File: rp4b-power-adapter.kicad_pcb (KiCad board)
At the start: 2 copper layers, 78 x 28 mm, 6 parts, among them X1 TYPE-C-31-M-12, X2 FH-00339

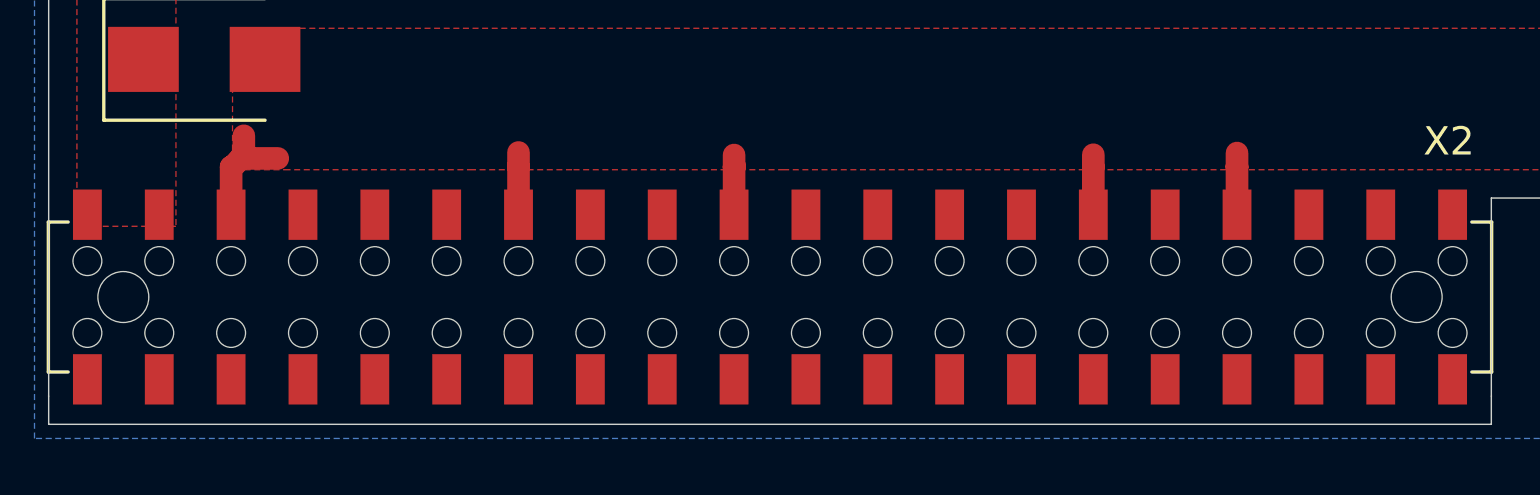
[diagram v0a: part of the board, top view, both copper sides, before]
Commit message: Add additional holes for FH-00369 and alternatives for FH-00339 (FH-00369, FH-00148)
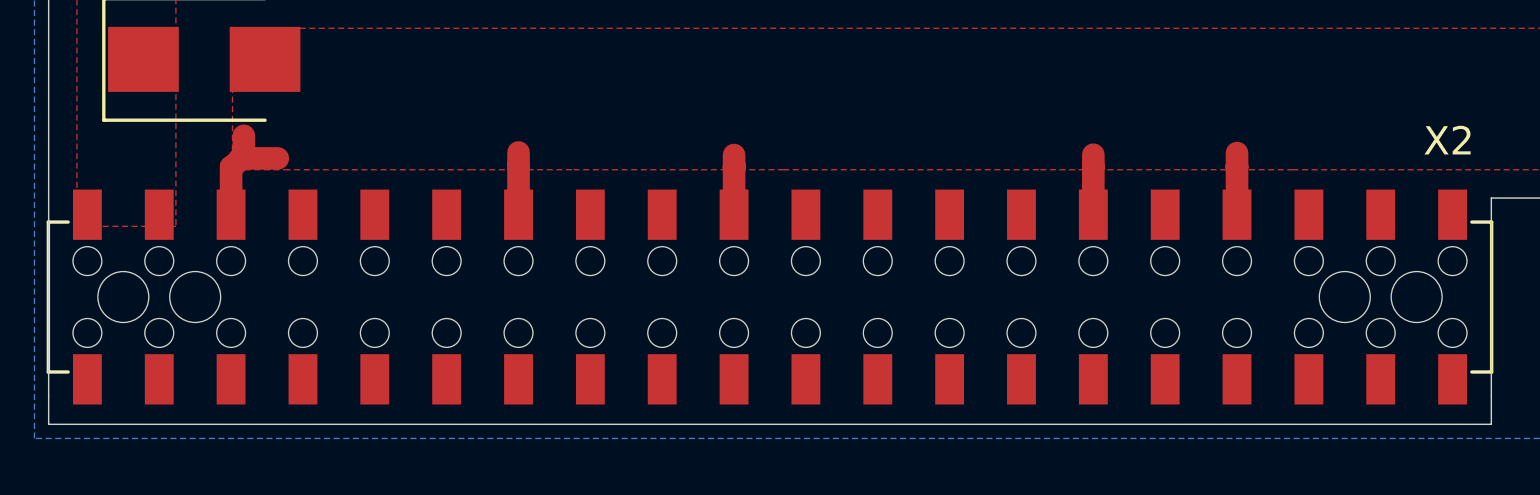
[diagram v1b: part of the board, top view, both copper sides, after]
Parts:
- added H2: FH-00369, Hole:Hole_1.8mm, F.Cu at (105.2, 96.5)
- added H3: FH-00369, Hole:Hole_1.8mm, F.Cu at (146.0, 96.5)
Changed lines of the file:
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@@
     (tracks 43)
     (zones 0)
-    (modules 6)
+    (modules 8)
     (nets 44)
   )
@@
     (mod_text_size 1 1)
     (mod_text_width 0.15)
-    (pad_size 1.524 1.524)
-    (pad_drill 0.762)
+    (pad_size 1.8 1.8)
+    (pad_drill 1.8)
     (pad_to_mask_clearance 0.051)
     (solder_mask_min_width 0.25)
@@
       (drillshape 0)
       (scaleselection 1)
-      (outputdirectory "gerber/"))
+      (outputdirectory "fabrication/"))
   )
   (net 0 "")
@@
     (add_net "Net-(X2-Pad9)")
   )
-  (module Connector_Harwin:Harwin_M20-7812045_2x20_P2.54mm_Vertical (layer F.Cu)
+  (module Hole:Hole_1.8mm locked (layer F.Cu)
+    (at 146 96.5)
+    (descr "Hole 1.8mm, no annular")
+    (tags "hole 1.8mm no annular")
+    (attr virtual)
+    (fp_text reference H3 (at -2.5 0) (layer F.SilkS) hide
+      (effects (font (size 1 1) (thickness 0.15)))
+    )
+    (fp_text value FH-00369 (at 0 2.1) (layer F.Fab)
+      (effects (font (size 1 1) (thickness 0.15)))
+    )
+    (fp_text user %R (at 0.3 0) (layer F.Fab)
+      (effects (font (size 1 1) (thickness 0.15)))
+    )
+    (pad "" np_thru_hole circle (at -0.18 0) (size 1.8 1.8) (drill 1.8) (layers *.Cu *.Mask))
+  )
+  (module Hole:Hole_1.8mm locked (layer F.Cu)
+    (at 105.18 96.5)
+    (descr "Hole 1.8mm, no annular")
+    (tags "hole 1.8mm no annular")
+    (attr virtual)
+    (fp_text reference H2 (at 2.32 0) (layer F.SilkS) hide
+      (effects (font (size 1 1) (thickness 0.15)))
+    )
+    (fp_text value FH-00369 (at 0 2.1) (layer F.Fab)
+      (effects (font (size 1 1) (thickness 0.15)))
+    )
+    (fp_text user %R (at 0.3 0) (layer F.Fab)
+      (effects (font (size 1 1) (thickness 0.15)))
+    )
+    (pad "" np_thru_hole circle (at 0 0) (size 1.8 1.8) (drill 1.8) (layers *.Cu *.Mask))
+  )
+  (module Connector_Harwin:Harwin_M20-7812045_2x20_P2.54mm_Vertical locked (layer F.Cu)
     (at 125.5 96.5 90)
     (descr "Harwin Female Vertical Surface Mount Double Row 2.54mm (0.1 inch) Pitch PCB Connector, M20-7812045, 20 Pins per row (https://cdn.harwin.com/pdfs/M20-781.pdf), generated with kicad-footprint-generator")
@@
     )
   )
-  (module MountingHole:MountingHole_2.7mm (layer F.Cu)
+  (module MountingHole:MountingHole_2.7mm locked (layer F.Cu)
     (at 154.5 83)
     (descr "Mounting Hole 2.7mm, no annular")
@@
     )
   )
-  (module Connector_USB:USB_C_Receptacle_HRO_TYPE-C-31-M-12 (layer F.Cu)
+  (module Connector_USB:USB_C_Receptacle_HRO_TYPE-C-31-M-12 locked (layer F.Cu)
     (at 175.75 83 90)
     (descr "USB Type-C receptacle for USB 2.0 and PD, http://www.krhro.com/uploads/soft/180320/1-1P320120243.pdf")
